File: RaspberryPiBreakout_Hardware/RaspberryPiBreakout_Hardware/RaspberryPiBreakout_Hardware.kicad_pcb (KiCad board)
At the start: 2 copper layers, 124.5 x 79.2 mm, 8 parts, among them U1 OKI, U2 Raspberry_Pi

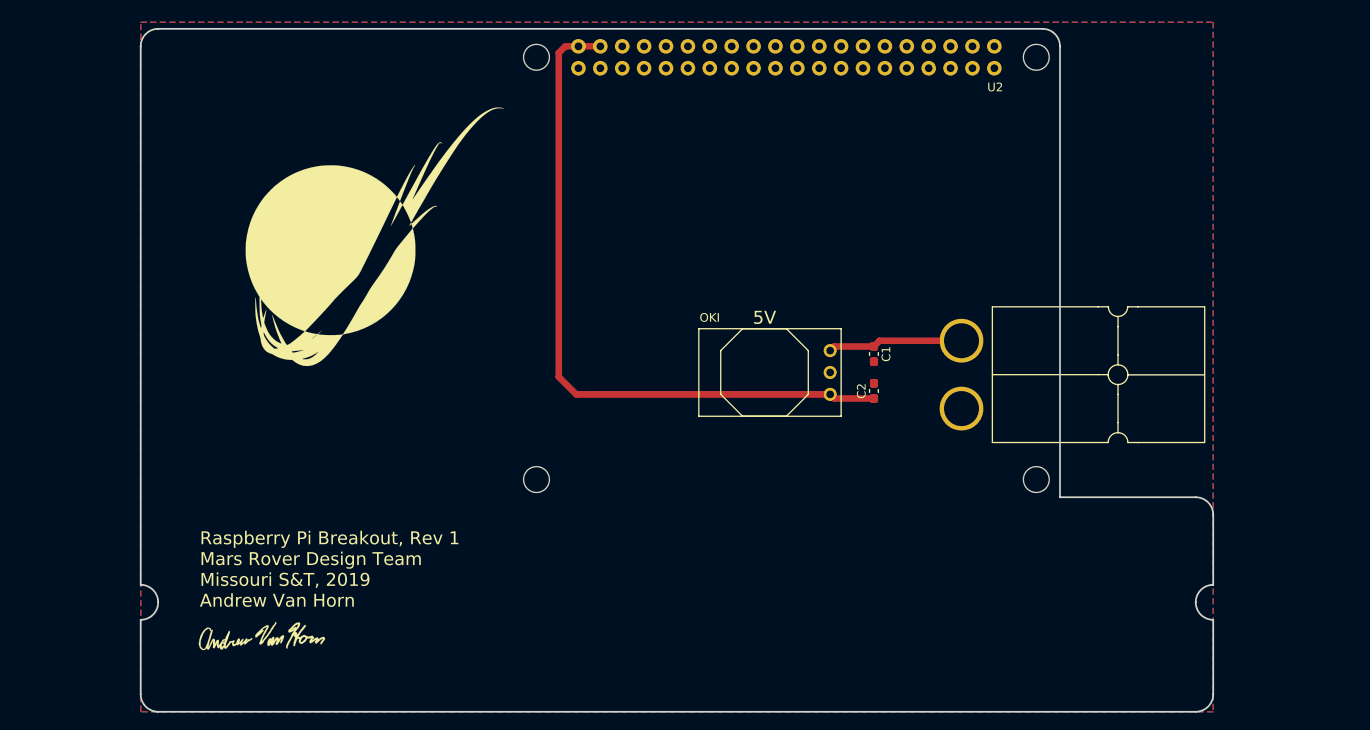
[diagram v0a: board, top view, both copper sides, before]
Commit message: annotated, net list, high level placement
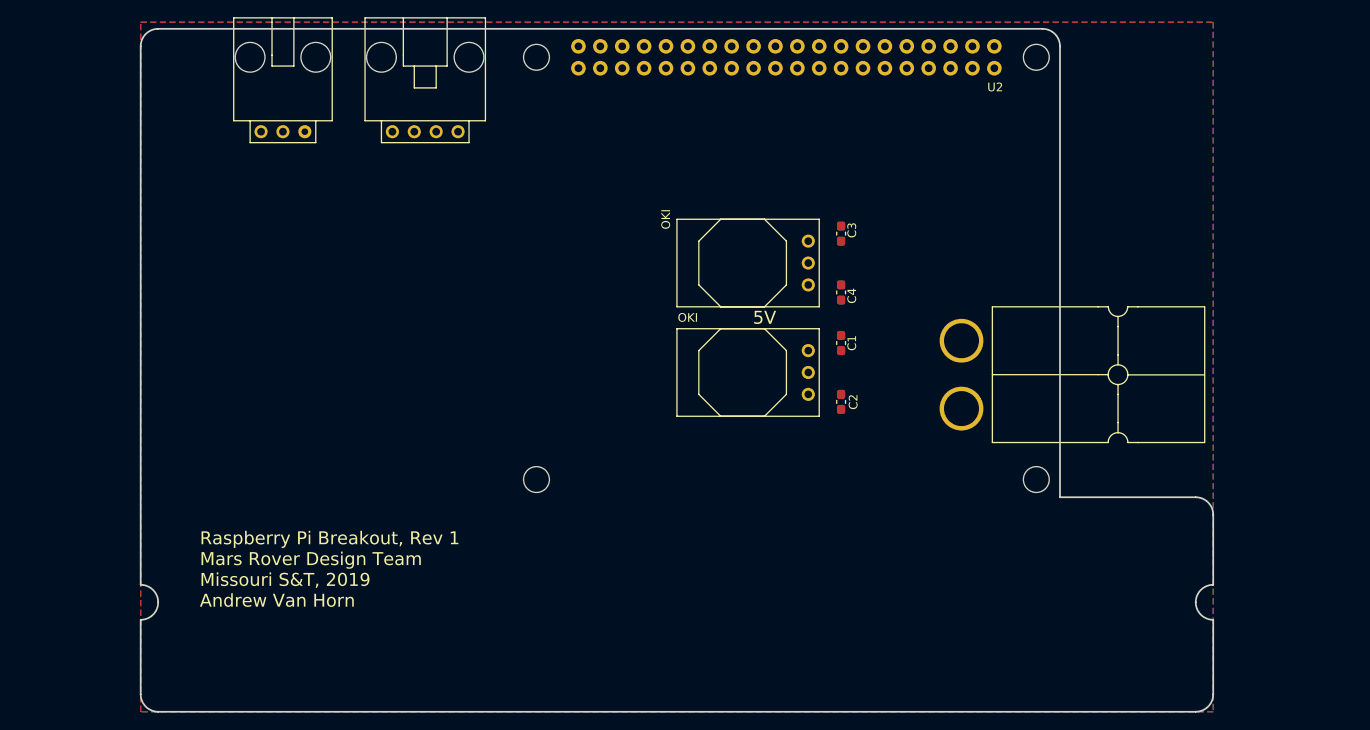
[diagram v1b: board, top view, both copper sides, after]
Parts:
- removed G***: LOGO, MRDT_Silkscreens:2_Dahlbot_2.0
- removed G***: LOGO, MRDT_Silkscreens:0_MRDT_Logo_30mm
- removed G***: LOGO, MRDT_Silkscreens:z_sig_Andrew_Van_Horn_Sig_15mm
- added C3: 10u, Capacitor_SMD:C_0603_1608Metric_Pad1.05x0.95mm_HandSolder, F.Cu at (153.7, 98.2)
- added C4: 10u, Capacitor_SMD:C_0603_1608Metric_Pad1.05x0.95mm_HandSolder, F.Cu at (153.7, 105.0)
- added Conn2: Molex_SL_03, MRDT_Connectors:MOLEX_SL_03_Horizontal, F.Cu at (88.9, 86.4)
- added Conn3: Molex_SL_04, MRDT_Connectors:MOLEX_SL_04_Horizontal, F.Cu at (105.4, 86.4)
- added U3: OKI, MRDT_Devices:OKI_Horizontal, F.Cu at (151.1, 96.5)
- moved C2 4.02 mm to (153.7, 117.7), turned to 270 degrees
- moved C1 4.02 mm to (153.7, 110.9), turned to 90 degrees
- moved U1 2.54 mm to (151.1, 109.2)
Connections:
- net Net-(C1-Pad1) renamed +12V
- U2 pad 1: Net-(U2-Pad1) -> +3V3
- U2 pad 10: Net-(U2-Pad10) -> Serial_Tx
- U2 pad 11: Net-(U2-Pad11) -> (no net)
- U2 pad 12: Net-(U2-Pad12) -> Serial_Rx
- U2 pad 13: Net-(U2-Pad13) -> (no net)
- U2 pad 15: Net-(U2-Pad15) -> (no net)
- U2 pad 16: Net-(U2-Pad16) -> (no net)
- U2 pad 17: Net-(U2-Pad17) -> +3V3
- U2 pad 19: Net-(U2-Pad19) -> (no net)
- U2 pad 21: Net-(U2-Pad21) -> (no net)
- U2 pad 22: Net-(U2-Pad22) -> (no net)
- U2 pad 23: Net-(U2-Pad23) -> (no net)
- U2 pad 24: Net-(U2-Pad24) -> (no net)
- U2 pad 26: Net-(U2-Pad26) -> (no net)
- U2 pad 27: Net-(U2-Pad27) -> (no net)
- U2 pad 28: Net-(U2-Pad28) -> (no net)
- U2 pad 29: Net-(U2-Pad29) -> (no net)
- U2 pad 3: Net-(U2-Pad3) -> SDA1
- U2 pad 31: Net-(U2-Pad31) -> (no net)
- U2 pad 32: Net-(U2-Pad32) -> (no net)
- U2 pad 33: Net-(U2-Pad33) -> (no net)
- U2 pad 35: Net-(U2-Pad35) -> (no net)
- U2 pad 36: Net-(U2-Pad36) -> (no net)
- U2 pad 37: Net-(U2-Pad37) -> (no net)
- U2 pad 38: Net-(U2-Pad38) -> (no net)
- U2 pad 40: Net-(U2-Pad40) -> (no net)
- U2 pad 5: Net-(U2-Pad5) -> SCL1
- U2 pad 7: Net-(U2-Pad7) -> (no net)
- U2 pad 8: Net-(U2-Pad8) -> (no net)
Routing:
- net +5V: track 80.4 -> 0.00 mm
- net +12V: track 15.7 -> 0.00 mm

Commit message: Added LED ind and gen new net list
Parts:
- added D1: LED, Diode_SMD:D_0603_1608Metric_Pad1.05x0.95mm_HandSolder, F.Cu at (204.9, 80.8)
- added D2: LED, Diode_SMD:D_0603_1608Metric_Pad1.05x0.95mm_HandSolder, F.Cu at (204.9, 82.4)
- added D3: LED, Diode_SMD:D_0603_1608Metric_Pad1.05x0.95mm_HandSolder, F.Cu at (208.3, 80.8)
- added D4: LED, Diode_SMD:D_0603_1608Metric_Pad1.05x0.95mm_HandSolder, F.Cu at (204.9, 84.0)
- added D5: LED, Diode_SMD:D_0603_1608Metric_Pad1.05x0.95mm_HandSolder, F.Cu at (208.3, 82.4)
- added R1: 500, Resistor_SMD:R_0603_1608Metric_Pad1.05x0.95mm_HandSolder, F.Cu at (204.9, 85.5)
- added R2: 500, Resistor_SMD:R_0603_1608Metric_Pad1.05x0.95mm_HandSolder, F.Cu at (211.7, 80.8)
- added R3: 500, Resistor_SMD:R_0603_1608Metric_Pad1.05x0.95mm_HandSolder, F.Cu at (208.3, 83.9)
- added R4: 500, Resistor_SMD:R_0603_1608Metric_Pad1.05x0.95mm_HandSolder, F.Cu at (211.7, 82.3)
- added R5: 500, Resistor_SMD:R_0603_1608Metric_Pad1.05x0.95mm_HandSolder, F.Cu at (208.3, 85.5)

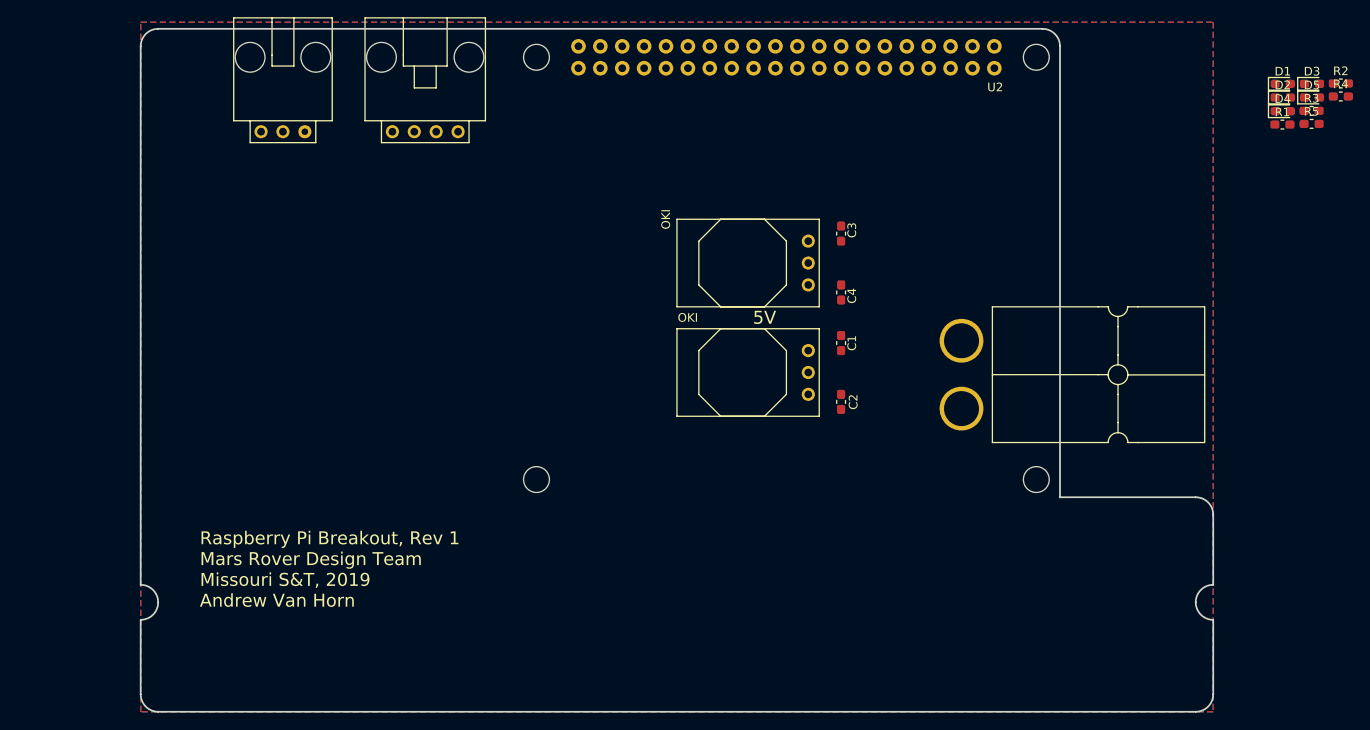
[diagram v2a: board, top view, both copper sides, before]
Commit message: High level layout placement
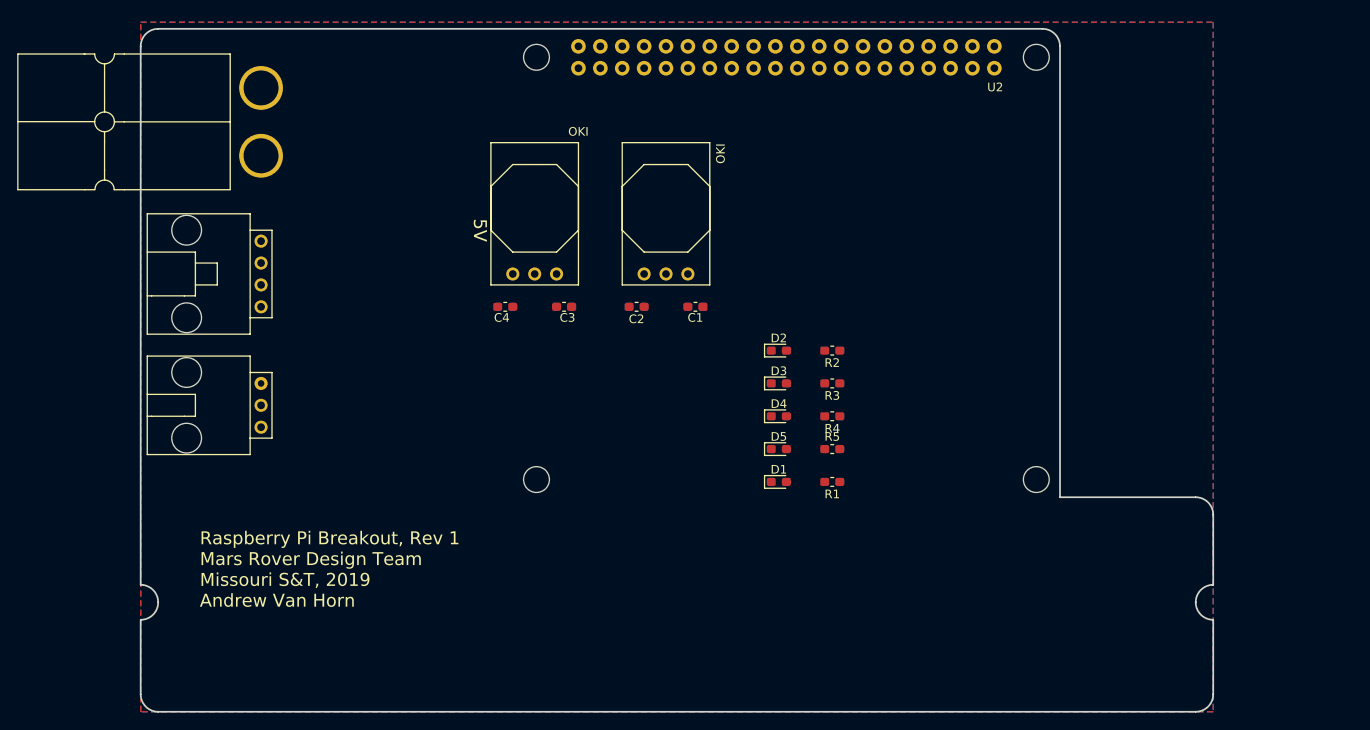
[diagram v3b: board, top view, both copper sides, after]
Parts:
- moved Conn1 89.5 mm to (82.8, 93.1), turned to 0 degrees
- moved D1 74.5 mm to (146.4, 127.0)
- moved D5 74.1 mm to (146.4, 123.2)
- moved D3 71.0 mm to (146.4, 115.6)
- moved R4 69.7 mm to (152.6, 119.4), turned to 180 degrees
- moved D4 68.4 mm to (146.4, 119.4)
- moved R5 67.2 mm to (152.6, 123.2)
- moved R1 66.7 mm to (152.6, 127.0), turned to 180 degrees
- moved R2 66.7 mm to (152.6, 111.8), turned to 180 degrees
- moved D2 65.4 mm to (146.4, 111.8)
- moved R3 64.0 mm to (152.6, 115.6), turned to 180 degrees
- moved C4 39.0 mm to (114.7, 106.7), turned to 180 degrees
- moved C3 33.2 mm to (121.5, 106.7), turned to 0 degrees
- moved Conn2 31.9 mm to (86.4, 118.1), turned to 90 degrees
- moved U3 29.0 mm to (123.2, 104.1), turned to 180 degrees
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
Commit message: Began traces
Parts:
- added C5: CP1, Capacitor_THT:CP_Radial_D6.3mm_P2.50mm, F.Cu at (107.3, 78.7)
- added R6: 4.7k, Resistor_SMD:R_0603_1608Metric_Pad1.05x0.95mm_HandSolder, F.Cu at (92.7, 105.8)
- added R7: 4.7k, Resistor_SMD:R_0603_1608Metric_Pad1.05x0.95mm_HandSolder, F.Cu at (89.5, 105.8)
- moved U1 27.2 mm to (116.8, 87.6), turned to 0 degrees
- moved D1 25.4 mm to (159.8, 105.4)
- moved D2 25.4 mm to (159.8, 90.2)
- moved D5 25.4 mm to (159.8, 101.6)
- moved R1 25.4 mm to (166.0, 105.4)
- moved R2 25.4 mm to (166.0, 90.2)
- moved R5 25.4 mm to (166.0, 101.6)
- moved D3 25.4 mm to (159.8, 94.0)
- moved D4 25.4 mm to (159.8, 97.8)
- moved R3 25.4 mm to (166.0, 94.0)
- moved R4 25.4 mm to (166.0, 97.8)
- moved C1 18.3 mm to (118.5, 106.0), turned to 180 degrees
- moved C3 8.28 mm to (113.3, 106.0)
- moved C4 8.28 mm to (106.4, 106.0)
- moved U3 8.25 mm to (114.9, 104.1)
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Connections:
- Conn3 pad 1: SDA1 -> +3V3
- Conn3 pad 2: SCL1 -> SDA1
- Conn3 pad 3: +3V3 -> SCL1
- U2 pad 10: Serial_Tx -> Serial_Rx
- U2 pad 12: Serial_Rx -> (no net)
- U2 pad 8: (no net) -> Serial_Tx
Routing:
- net +3V3: track 0.00 -> 96.6 mm, vias 0 -> 5
- net +12V: track 0.00 -> 67.3 mm
- net +5V: track 0.00 -> 33.8 mm
- net SCL1: track 0.00 -> 9.31 mm
- net SDA1: track 0.00 -> 3.50 mm
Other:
- board text added: "3.3V"

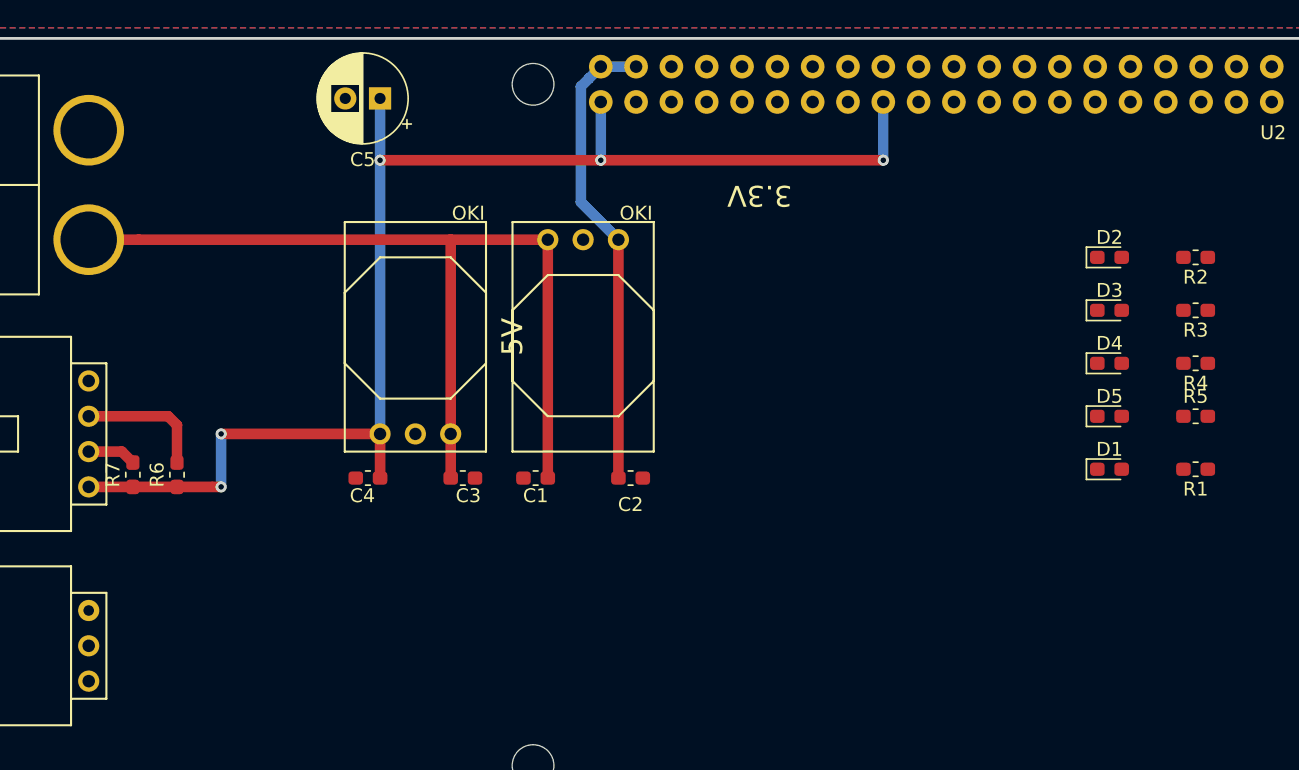
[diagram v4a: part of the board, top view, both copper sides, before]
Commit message: Layout and traces complete
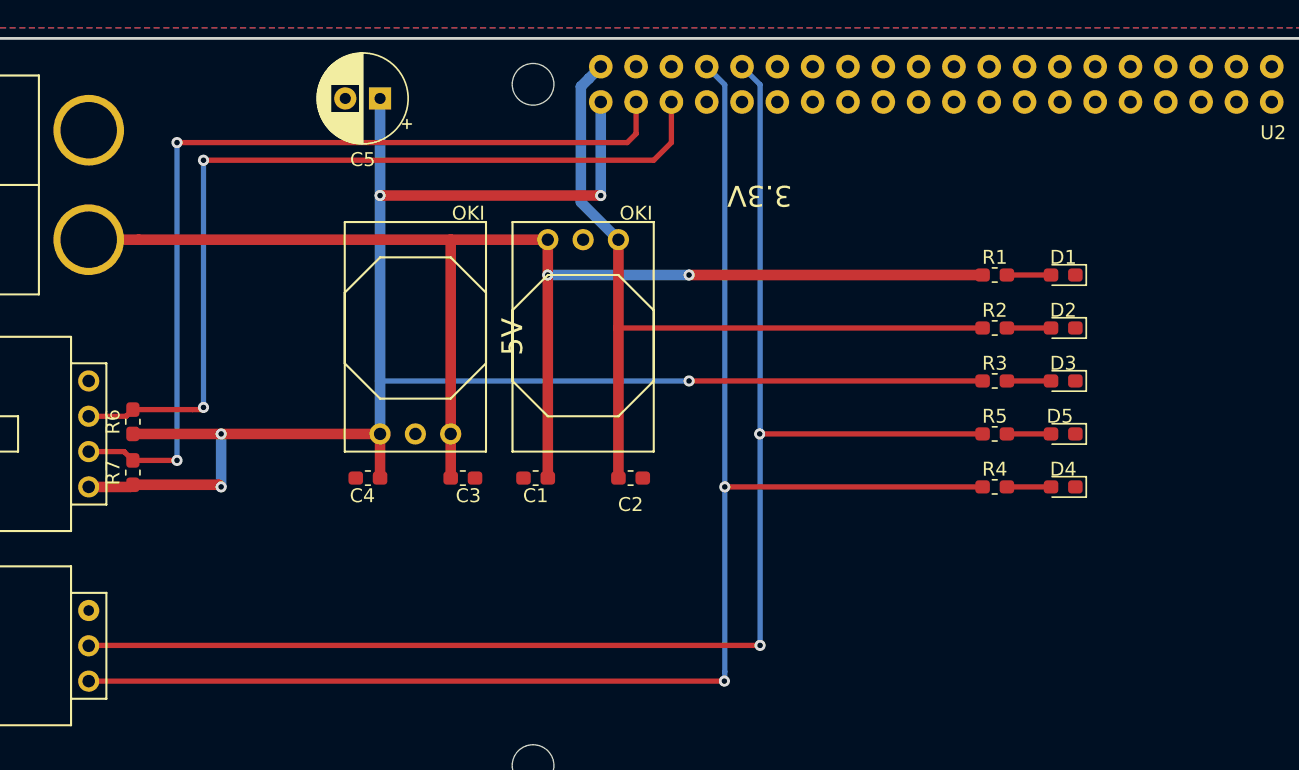
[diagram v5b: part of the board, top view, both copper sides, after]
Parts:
- moved R1 20.1 mm to (151.5, 91.4), turned to 0 degrees
- moved R4 17.0 mm to (151.5, 106.7), turned to 0 degrees
- moved R2 15.3 mm to (151.5, 95.2), turned to 0 degrees
- moved R3 15.3 mm to (151.5, 99.1), turned to 0 degrees
- moved R5 14.5 mm to (151.5, 102.9)
- moved D1 14.4 mm to (156.4, 91.4), turned to 180 degrees
- moved D4 9.49 mm to (156.4, 106.7), turned to 180 degrees
- moved D2 6.07 mm to (156.4, 95.2), turned to 180 degrees
- moved D3 6.07 mm to (156.4, 99.1), turned to 180 degrees
- moved R6 4.96 mm to (89.5, 102.0)
- moved D5 3.56 mm to (156.4, 102.9), turned to 180 degrees
- moved R7 0.16 mm to (89.5, 105.7)
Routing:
- net Serial_Tx: track 0.00 -> 109.0 mm, vias 0 -> 2
- net Serial_Rx: track 0.00 -> 106.5 mm, vias 0 -> 2
- net SDA1: track 3.50 -> 65.0 mm, vias 0 -> 2
- net SCL1: track 9.31 -> 63.4 mm, vias 0 -> 2
- net +12V: track 67.3 -> 98.6 mm, vias 0 -> 2
- net +3V3: track 96.6 -> 124.5 mm
- net +5V: track 33.8 -> 57.5 mm
- net Net-(D5-Pad2): track 0.00 -> 3.17 mm
- net Net-(D4-Pad2): track 0.00 -> 3.17 mm
- net Net-(D3-Pad2): track 0.00 -> 3.17 mm
- net Net-(D2-Pad2): track 0.00 -> 3.17 mm
- net Net-(D1-Pad2): track 0.00 -> 3.17 mm
